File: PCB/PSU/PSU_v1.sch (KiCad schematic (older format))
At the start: 19 parts, among them J1 CONN_01X05, Q1 MPSA55, Q2 IRF630, U1 MC34063

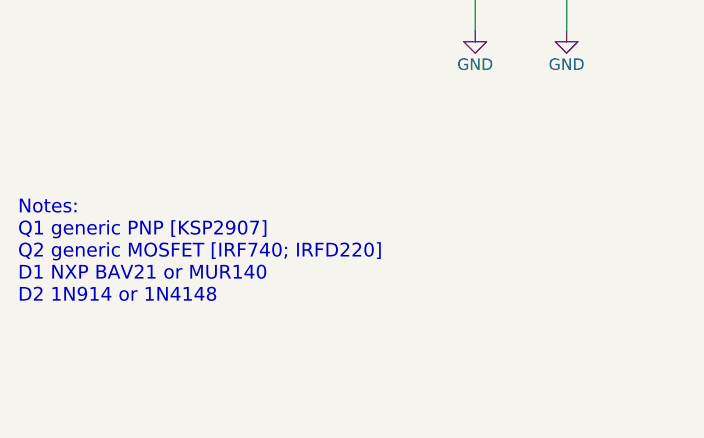
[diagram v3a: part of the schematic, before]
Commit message: Some tweaks to schematic and PCB based on laser etching prototyping
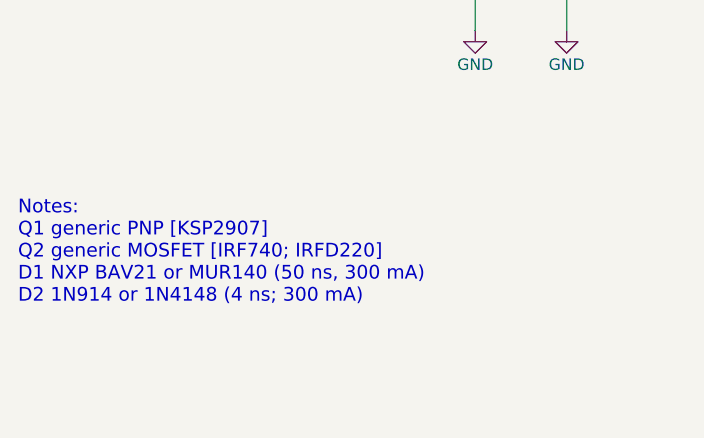
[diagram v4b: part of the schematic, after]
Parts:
- D2: footprint Diodes_SMD:D_SOD-323 -> Diodes_SMD:D_SOD-123
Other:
- note added: "Notes:\nQ1 generic PNP [KSP2907]\nQ2 generic MOSFET [IRF740; IRFD220]\nD1 NXP BAV21 or MUR140 (50 ns, 300 mA)\nD2 1N914 or 1N4148 (4 ns; 300 mA)"
- note removed: "Notes:\nQ1 generic PNP [KSP2907]\nQ2 generic MOSFET [IRF740; IRFD220]\nD1 NXP BAV21 or MUR140\nD2 1N914 or 1N4148"
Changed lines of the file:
@@
 F 0 "D2" H 6900 2950 50  0000 C CNN
 F 1 "BAV21" H 6900 2750 50  0000 C CNN
-F 2 "Diodes_SMD:D_SOD-323" H 6900 2850 50  0001 C CNN
+F 2 "Diodes_SMD:D_SOD-123" H 6900 2850 50  0001 C CNN
 F 3 "" H 6900 2850 50  0000 C CNN
 	1    6900 2850
@@
 Connection ~ 6500 2850
 Text Notes 1150 5500 0    60   ~ 0
-Notes:\nQ1 generic PNP [KSP2907]\nQ2 generic MOSFET [IRF740; IRFD220]\nD1 NXP BAV21 or MUR140\nD2 1N914 or 1N4148
+Notes:\nQ1 generic PNP [KSP2907]\nQ2 generic MOSFET [IRF740; IRFD220]\nD1 NXP BAV21 or MUR140 (50 ns, 300 mA)\nD2 1N914 or 1N4148 (4 ns; 300 mA)
 $Comp
 L GND #PWR012

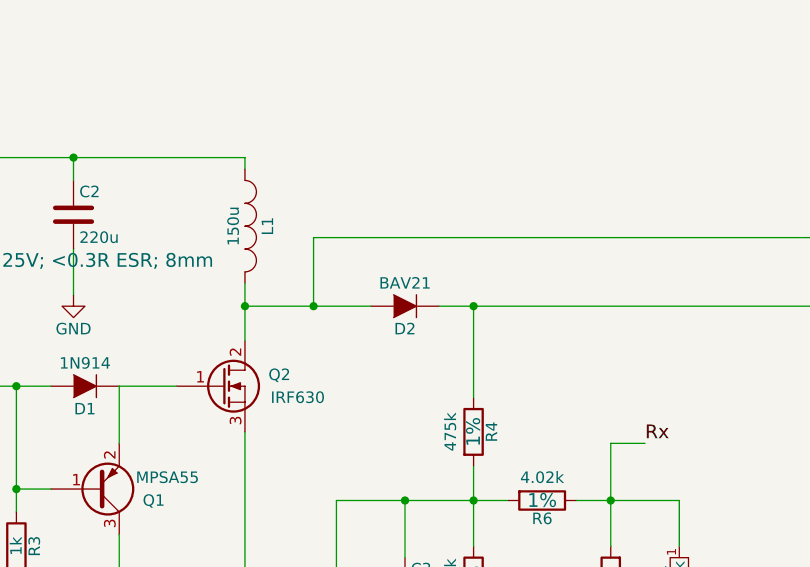
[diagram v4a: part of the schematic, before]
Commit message: Edits to some component footprints due to component availability
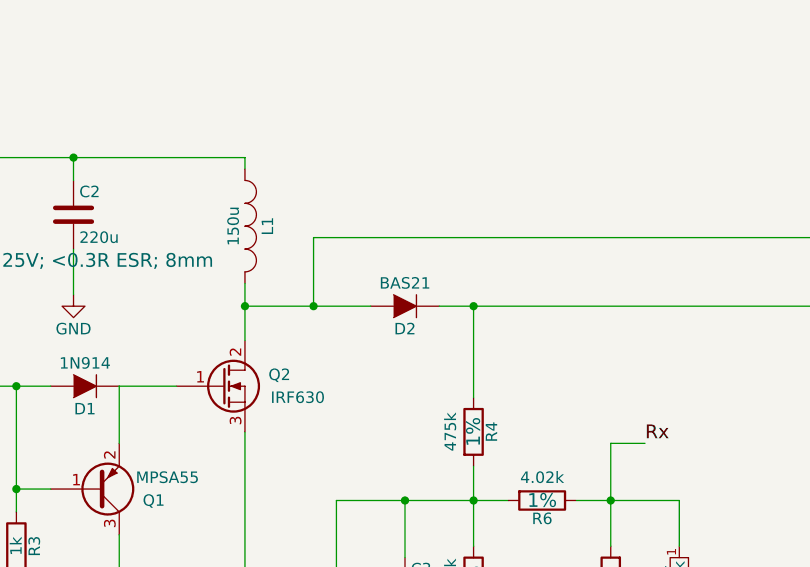
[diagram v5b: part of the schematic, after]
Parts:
- removed D2: BAV21, Diodes_SMD:D_SOD-123, symbol D
- added D2: BAS21, TO_SOT_Packages_SMD:SOT-23_Handsoldering, symbol BAS21
- R4, R5: footprint Resistors_SMD:R_0805_HandSoldering -> Resistors_SMD:R_0603_HandSoldering
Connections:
- net Vout: now also D2.3 (K)
- net Vpulse: now also D2.1 (A)
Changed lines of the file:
@@
 F 1 "0.5R" V 3900 2450 50  0000 C CNN
 F 2 "Resistors_SMD:R_1210_HandSoldering" V 3830 2450 50  0001 C CNN
-F 3 "" H 3900 2450 50  0000 C CNN
+F 3 "https://www.elfa.se/en/precision-resistor-smd-51-ohm-33-1206-panasonic-automotive-industrial-systems-erj8bqfr51v/p/16033314" H 3900 2450 50  0001 C CNN
 	1    3900 2450
 	0    1    1    0
@@
 F 1 "0.5R" V 3900 2200 50  0000 C CNN
 F 2 "Resistors_SMD:R_1210_HandSoldering" V 3830 2200 50  0001 C CNN
-F 3 "" H 3900 2200 50  0000 C CNN
+F 3 "https://www.elfa.se/en/precision-resistor-smd-51-ohm-33-1206-panasonic-automotive-industrial-systems-erj8bqfr51v/p/16033314" H 3900 2200 50  0001 C CNN
 	1    3900 2200
 	0    1    1    0
@@
 F 1 "220u" H 5475 2350 50  0000 L CNN
 F 2 "Capacitors_SMD:CP_Elec_8x10.5" H 5488 2300 50  0001 C CNN
-F 3 "" H 5450 2450 50  0000 C CNN
+F 3 "https://www.elfa.se/en/aluminium-electrolytic-capacitor-330-uf-suncon-25ce330lx/p/16720387" H 5450 2450 50  0001 C CNN
 F 4 "25V; <0.3R ESR; 8mm" H 5600 2250 60  0000 C CNN "Field4"
 	1    5450 2450
@@
 F 1 "1k" V 5200 3900 50  0000 C CNN
 F 2 "Resistors_SMD:R_0805_HandSoldering" V 5130 3900 50  0001 C CNN
-F 3 "" H 5200 3900 50  0000 C CNN
+F 3 "https://www.elfa.se/en/smd-resistor-thick-film-kohm-0805-rnd-components-rnd-1550805s8j0102t5e/p/30056853" H 5200 3900 50  0001 C CNN
 	1    5200 3900
 	1    0    0    -1
@@
 F 1 "1N914" H 5500 3100 50  0000 C CNN
 F 2 "Diodes_SMD:D_SOD-123" H 5500 3200 50  0001 C CNN
-F 3 "" H 5500 3200 50  0000 C CNN
+F 3 "https://www.elfa.se/en/diode-sod-123-75-diotec-1n4148w/p/17000727" H 5500 3200 50  0001 C CNN
 	1    5500 3200
 	-1   0    0    1
@@
 Connection ~ 6200 2850
 $Comp
-L D D2
-U 1 1 589B70C6
-P 6900 2850
-F 0 "D2" H 6900 2950 50  0000 C CNN
-F 1 "BAV21" H 6900 2750 50  0000 C CNN
-F 2 "Diodes_SMD:D_SOD-123" H 6900 2850 50  0001 C CNN
-F 3 "" H 6900 2850 50  0000 C CNN
-	1    6900 2850
-	-1   0    0    1
-$EndComp
-$Comp
 L R R4
 U 1 1 589B749B
@@
 F 0 "R4" V 7280 3400 50  0000 C CNN
 F 1 "475k" V 7100 3400 50  0000 C CNN
-F 2 "Resistors_SMD:R_0805_HandSoldering" V 7130 3400 50  0001 C CNN
-F 3 "" H 7200 3400 50  0000 C CNN
+F 2 "Resistors_SMD:R_0603_HandSoldering" V 7130 3400 50  0001 C CNN
+F 3 "https://www.elfa.se/en/smd-resistor-thick-film-475-kohm-0603-rnd-components-rnd-1550603saf4753t5e/p/30056615" H 7200 3400 50  0001 C CNN
 F 4 "1%" V 7200 3400 60  0000 C CNN "Field4"
 	1    7200 3400
@@
 F 0 "R5" V 7280 4050 50  0000 C CNN
 F 1 "13.7k" V 7100 4050 50  0000 C CNN
-F 2 "Resistors_SMD:R_0805_HandSoldering" V 7130 4050 50  0001 C CNN
-F 3 "" H 7200 4050 50  0000 C CNN
+F 2 "Resistors_SMD:R_0603_HandSoldering" V 7130 4050 50  0001 C CNN
+F 3 "https://www.elfa.se/en/precision-resistor-smd-13-kohm-0603-panasonic-automotive-industrial-systems-erj3ekf1372v/p/30051398" H 7200 4050 50  0001 C CNN
 F 4 "1%" V 7200 4050 60  0000 C CNN "Field4"
 	1    7200 4050
@@
 F 1 "0.01u" H 6925 4000 50  0000 L CNN
 F 2 "Capacitors_SMD:C_0805_HandSoldering" H 6938 3950 50  0001 C CNN
-F 3 "" H 6900 4100 50  0000 C CNN
+F 3 "https://www.elfa.se/en/capacitor-10-nf-0805-rnd-components-rnd-1500805b103k500/p/30065754" H 6900 4100 50  0001 C CNN
 F 4 "50V" H 7000 3900 60  0000 C CNN "Field4"
 	1    6900 4100
@@
 F 1 "2.2u" H 8825 3100 50  0000 L CNN
 F 2 "Capacitors_SMD:CP_Elec_10x10.5" H 8838 3050 50  0001 C CNN
-F 3 "" H 8800 3200 50  0000 C CNN
+F 3 "https://www.elfa.se/en/aluminium-electrolytic-capacitor-uf-suncon-250ce6r8fs/p/16722532" H 8800 3200 50  0001 C CNN
 F 4 "250V" H 8950 3000 60  0000 C CNN "Field4"
 	1    8800 3200
@@
 F 1 "4.02k" V 7400 3700 50  0000 C CNN
 F 2 "Resistors_SMD:R_0805_HandSoldering" V 7430 3700 50  0001 C CNN
-F 3 "" H 7500 3700 50  0000 C CNN
+F 3 "https://www.elfa.se/en/precision-resistor-smd-02-kohm-125-0805-panasonic-automotive-industrial-systems-erj6enf4021v/p/30051502" H 7500 3700 50  0001 C CNN
 F 4 "1%" V 7500 3700 60  0000 C CNN "Field4"
 	1    7500 3700
@@
 F 1 "IRF630" H 6550 3150 50  0000 R CNN
 F 2 "TO_SOT_Packages_SMD:TO-252-2Lead" H 6300 3300 50  0001 C CNN
-F 3 "" H 6100 3200 50  0000 C CNN
+F 3 "https://www.elfa.se/en/mosfet-400-10-125-d2pak-vishay-irf740spbf/p/17115868" H 6100 3200 50  0001 C CNN
 	1    6100 3200
 	1    0    0    -1
@@
 Text Label 8950 1250 2    60   ~ 0
 Vpulse
+$Comp
+L BAS21 D2
+U 1 1 58A781C3
+P 6900 2850
+F 0 "D2" H 6900 2950 50  0000 C CNN
+F 1 "BAS21" H 6900 2750 50  0000 C CNN
+F 2 "TO_SOT_Packages_SMD:SOT-23_Handsoldering" H 6900 2850 50  0001 C CNN
+F 3 "https://www.elfa.se/en/diode-sot-23-200-infineon-bas21/p/17030082" H 6900 2850 50  0001 C CNN
+	1    6900 2850
+	-1   0    0    1
+$EndComp
 $EndSCHEMATC

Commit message: Newer KiCad format and gitignore for LTSpice
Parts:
- U1: symbol MC34063 -> MC34063-RESCUE-PSU_v1
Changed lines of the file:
@@
 EESchema Schematic File Version 2
+LIBS:PSU_v1-rescue
 LIBS:device
 LIBS:power
@@
 $EndDescr
 $Comp
-L MC34063 U1
+L MC34063-RESCUE-PSU_v1 U1
 U 1 1 589B59F5
 P 4350 3150
